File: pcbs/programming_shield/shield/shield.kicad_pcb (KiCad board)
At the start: 2 copper layers, 68.6 x 53.3 mm, 8 parts, among them P1 Power, P2 Analog, P3 Digital, P4 Digital, P5 CONN_01X01, P6 CONN_01X01, P7 CONN_01X01, P8 CONN_01X01

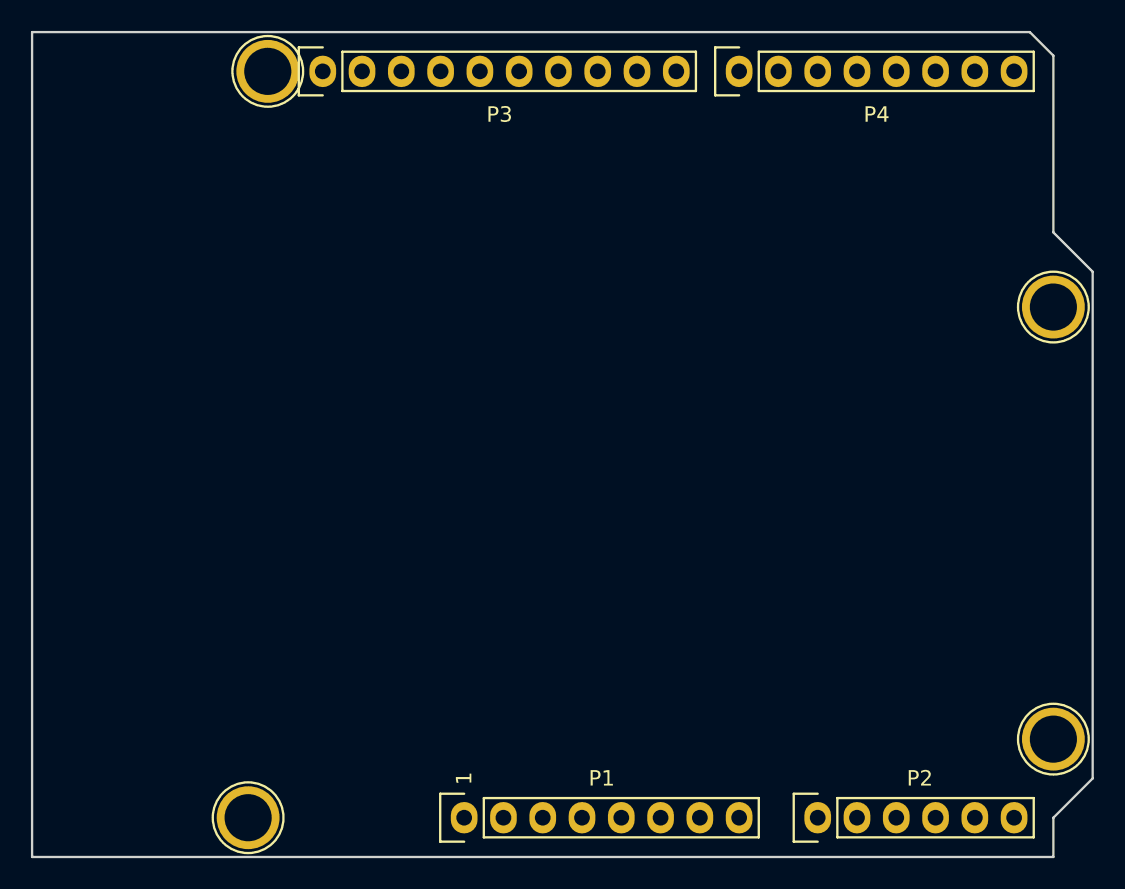
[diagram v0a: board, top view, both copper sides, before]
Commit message: produced PCBs, dropped baudrate, removed on-board dynamic address selection - decoder must now be configured via programmer!
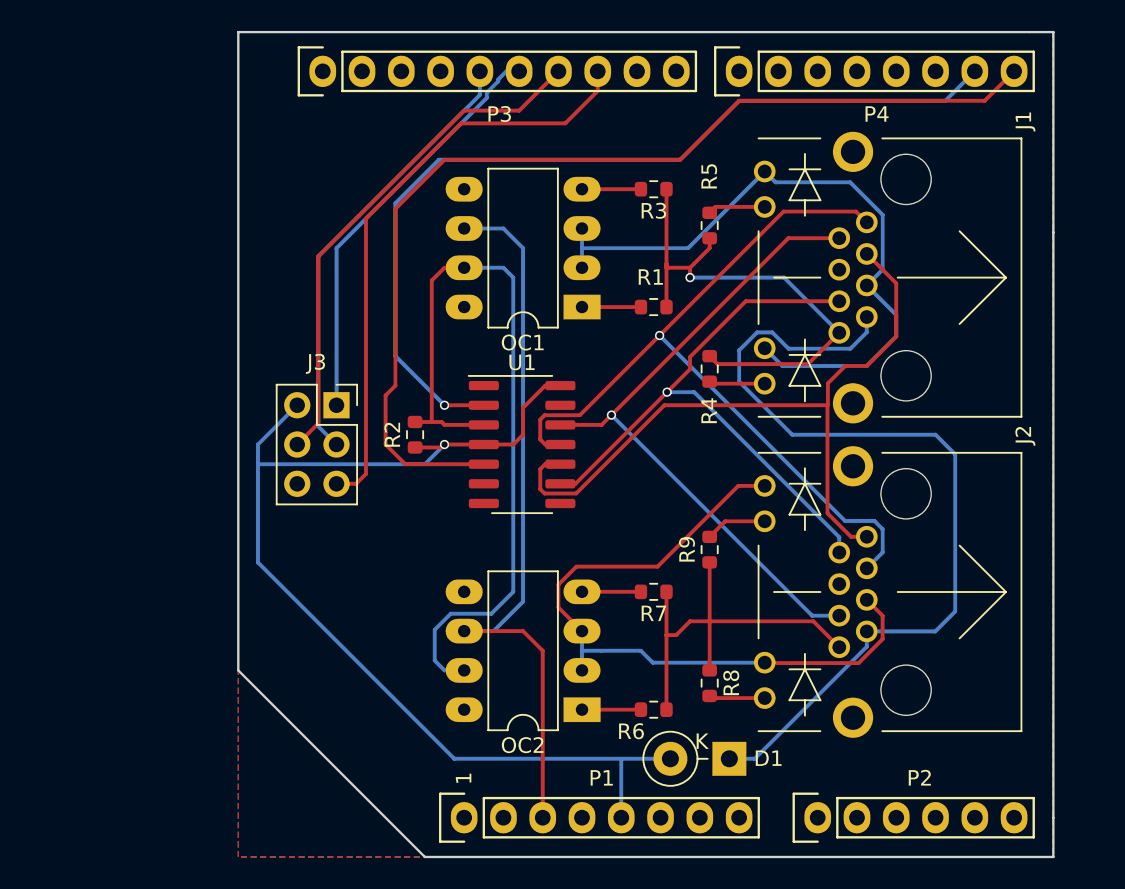
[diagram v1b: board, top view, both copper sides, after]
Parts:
- removed P5, P6, P7, P8: CONN_01X01, Socket_Arduino_Uno:Arduino_1pin
- added D1: 1N4001, Diode_THT:D_DO-41_SOD81_P3.81mm_Vertical_KathodeUp, F.Cu at (156.1, 120.0)
- added J1: RJ45_LED, customs:RND_RJ45_LED, F.Cu at (165.0, 88.9)
- added J2: RJ45_LED, customs:RND_RJ45_LED, F.Cu at (165.0, 109.2)
- added J3: AVR-ISP-6, Connector_PinSocket_2.54mm:PinSocket_2x03_P2.54mm_Vertical, F.Cu at (130.7, 97.2)
- added OC1: CNY74-2H, Package_DIP:DIP-8_W7.62mm_LongPads, F.Cu at (146.6, 90.8)
- added OC2: CNY74-2H, Package_DIP:DIP-8_W7.62mm_LongPads, F.Cu at (146.6, 116.8)
- added R1: R, Resistor_SMD:R_0603_1608Metric, F.Cu at (151.2, 90.8)
- added R2: R, Resistor_SMD:R_0603_1608Metric, F.Cu at (135.8, 99.1)
- added R3: R, Resistor_SMD:R_0603_1608Metric, F.Cu at (151.2, 83.2)
- added R4: R, Resistor_SMD:R_0603_1608Metric, F.Cu at (154.8, 94.8)
- added R5: R, Resistor_SMD:R_0603_1608Metric, F.Cu at (154.8, 85.5)
- added R6: R, Resistor_SMD:R_0603_1608Metric, F.Cu at (151.2, 116.8)
- added R7: R, Resistor_SMD:R_0603_1608Metric, F.Cu at (151.2, 109.2)
- added R8: R, Resistor_SMD:R_0603_1608Metric, F.Cu at (154.8, 115.1)
- added R9: R, Resistor_SMD:R_0603_1608Metric, F.Cu at (154.8, 106.5)
- added U1: MAX489E, Package_SO:SOIC-14_3.9x8.7mm_P1.27mm, F.Cu at (142.7, 99.7)
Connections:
- P1 pad 1: Net-(P1-Pad1) -> (no net)
- P1 pad 2: /IOREF -> (no net)
- P1 pad 4: +3V3 -> (no net)
- P1 pad 5: +5V -> 5V
- P1 pad 8: /Vin -> (no net)
- P2 pad 1: /A0 -> (no net)
- P2 pad 2: /A1 -> (no net)
- P2 pad 3: /A2 -> (no net)
- P2 pad 4: /A3 -> (no net)
- P3 pad 10: /8 -> (no net)
- P3 pad 3: /AREF -> (no net)
- P3 pad 9: /9(**) -> (no net)
- P4 pad 1: /7 -> (no net)
- P4 pad 2: /6(**) -> (no net)
- P4 pad 3: /5(**) -> (no net)
- P4 pad 4: /4 -> (no net)
- P4 pad 5: /3(**) -> (no net)
- P4 pad 6: /2 -> (no net)
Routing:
- net 5V: track 0.00 -> 71.6 mm, vias 0 -> 1
- net /0(Rx): track 0.00 -> 66.1 mm
- net /1(Tx): track 0.00 -> 57.9 mm, vias 0 -> 1
- net Net-(D1-Pad1): track 0.00 -> 57.8 mm
- net Net-(J1-Pad1): track 0.00 -> 52.3 mm, vias 0 -> 1
- net Net-(OC1-Pad7): track 0.00 -> 50.1 mm
- net /Reset: track 0.00 -> 48.2 mm
- net Net-(J1-Pad3): track 0.00 -> 47.2 mm
- net /sense-B: track 0.00 -> 45.5 mm
- net /sense-: track 0.00 -> 44.0 mm
- net Net-(J1-Pad2): track 0.00 -> 43.1 mm, vias 0 -> 1
- net Net-(J1-Pad6): track 0.00 -> 39.4 mm, vias 0 -> 1
- net /10(**/SS): track 0.00 -> 38.4 mm
- net /11(**/MOSI): track 0.00 -> 33.2 mm
- net /sense+: track 0.00 -> 33.0 mm, vias 0 -> 1
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- added copper zone on B.Cu, net GND
- added copper zone on F.Cu, net GND
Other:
- board size 68.6 x 53.3 mm -> 52.7 x 53.3 mm
